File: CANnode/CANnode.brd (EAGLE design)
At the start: 59.8 x 57.7 mm, 244 parts, among them IC1 ISO1050DUB, IC2 ISO1050DUB, Q1 FDV302P, Q3 FDV302P, U1 LM324PW, U10 FT2232HL, U11 93LC56C-I/SN, U2 TPS70445_PWP_24, U3 LM324PW, U4 LM324PW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

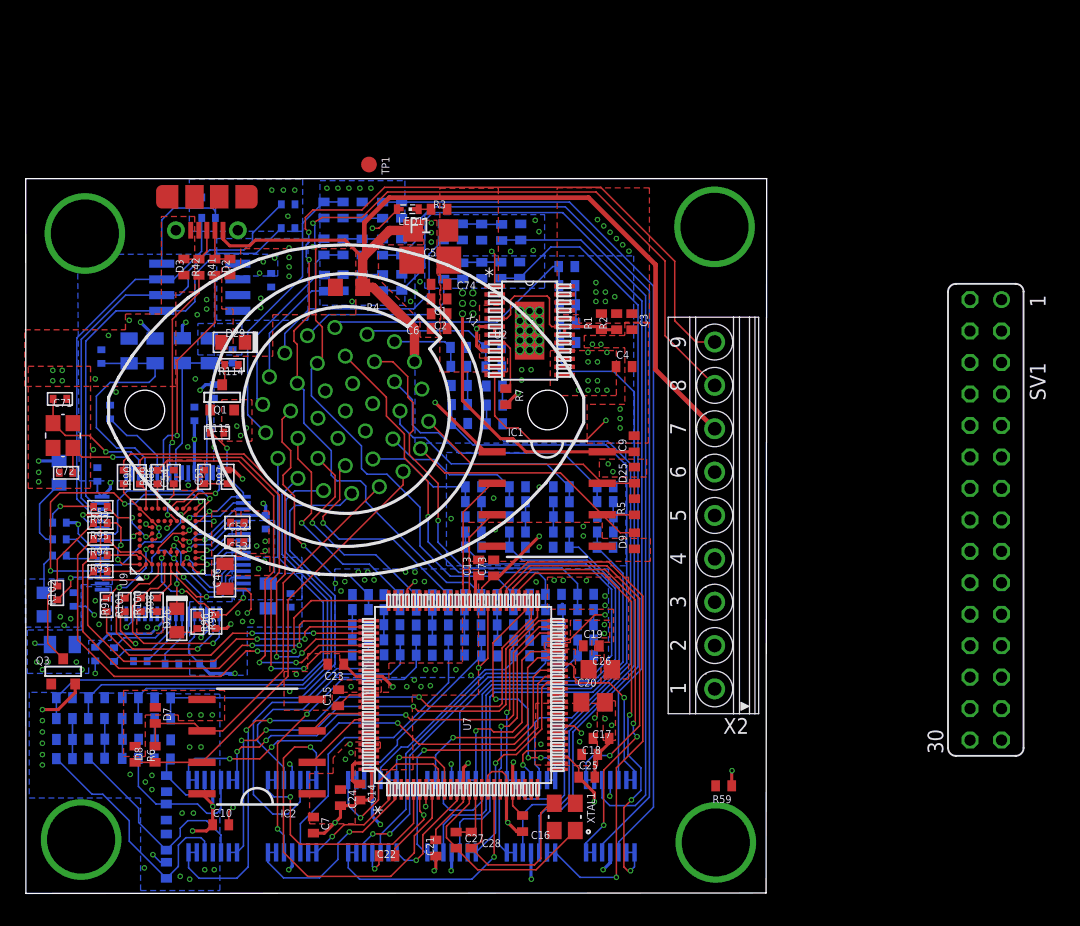
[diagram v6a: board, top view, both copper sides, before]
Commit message: Finished Debug headers
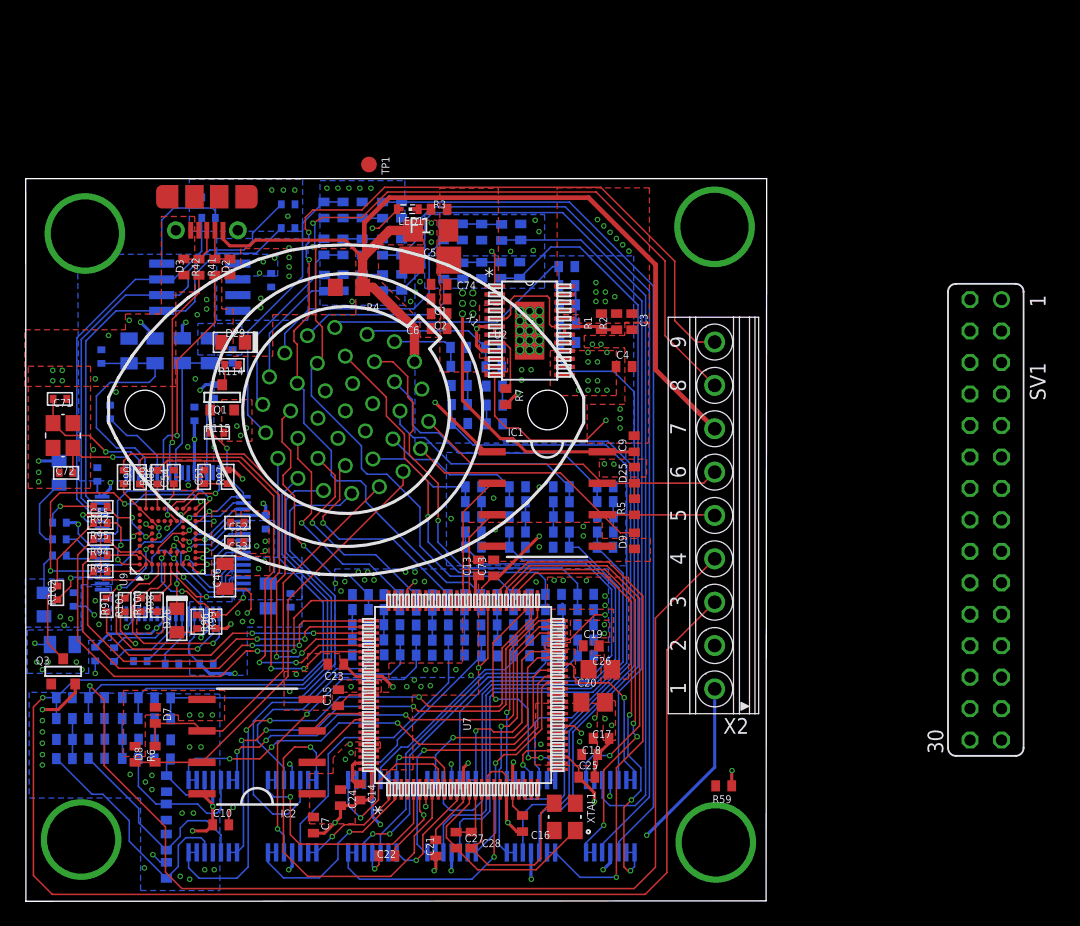
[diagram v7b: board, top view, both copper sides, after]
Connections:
- removed net N$44: X2.6
- removed net N$69: X2.5
- removed net N$70: X2.4
- removed net N$71: X2.3
- removed net N$72: X2.2
- net +5V: now also X2.1
- net A2_IN: now also X2.4
- net A3_IN: now also X2.3
- net CAN1H: now also X2.6
- net CAN1L: now also X2.5
- net GND: now also X2.2; no longer X2.1
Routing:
- net A3_IN: track 42.3 -> 134.0 mm, vias 0 -> 1
- net A2_IN: track 39.0 -> 125.2 mm, vias 0 -> 1
- net +5V: track 40.4 -> 54.4 mm, vias 13 -> 14
- net CAN1H: track 19.9 -> 26.8 mm
- net CAN1L: track 22.7 -> 29.2 mm
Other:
- board size 59.8 x 57.7 mm -> 59.8 x 58.3 mm
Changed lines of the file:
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@@
 <setting verticaltext="up"/>
 </settings>
-<grid distance="3" unitdist="mil" unit="mil" style="lines" multiple="1" display="no" altdistance="0.025" altunitdist="inch" altunit="mil"/>
+<grid distance="1" unitdist="mil" unit="mil" style="lines" multiple="1" display="no" altdistance="0.025" altunitdist="inch" altunit="mil"/>
 <layers>
 <layer number="1" name="Top" color="12" fill="1" visible="yes" active="yes"/>
@@
 <board>
 <plain>
-<wire x1="0.001153125" y1="-0.000778125" x2="59.747884375" y2="0.034490625" width="0" layer="20"/>
-<wire x1="59.747884375" y1="0.034490625" x2="59.795128125" y2="57.6990375" width="0" layer="20"/>
+<wire x1="0.001153125" y1="-0.635778125" x2="59.747884375" y2="-0.600509375" width="0" layer="20"/>
+<wire x1="59.747884375" y1="-0.600509375" x2="59.795128125" y2="57.6990375" width="0" layer="20"/>
 <wire x1="59.795128125" y1="57.6990375" x2="-0.01470625" y2="57.694140625" width="0" layer="20"/>
-<wire x1="-0.01470625" y1="57.694140625" x2="0.001153125" y2="-0.000778125" width="0" layer="20"/>
+<wire x1="-0.01470625" y1="57.694140625" x2="0.001153125" y2="-0.635778125" width="0" layer="20"/>
 </plain>
 <attributes>
@@
 <wire x1="46.52205625" y1="33.10653125" x2="49.1140625" y2="33.10653125" width="0.127" layer="1"/>
 <wire x1="49.1140625" y1="33.10653125" x2="49.120021875" y2="33.114165625" width="0.127" layer="1"/>
+<contactref element="X2" pad="6"/>
+<wire x1="49.120021875" y1="33.114165625" x2="54.705665625" y2="33.114165625" width="0.127" layer="1"/>
+<wire x1="54.705665625" y1="33.114165625" x2="55.599" y2="34.0075" width="0.127" layer="1"/>
 </signal>
 <signal name="CAN1L">
@@
 <wire x1="49.124909375" y1="30.55805" x2="46.5305375" y2="30.55805" width="0.127" layer="1"/>
 <wire x1="46.5305375" y1="30.55805" x2="46.52205625" y2="30.56653125" width="0.127" layer="1"/>
+<contactref element="X2" pad="5"/>
+<wire x1="49.124909375" y1="30.55805" x2="55.54845" y2="30.55805" width="0.127" layer="1"/>
+<wire x1="55.54845" y1="30.55805" x2="55.599" y2="30.5075" width="0.127" layer="1"/>
 </signal>
 <signal name="CAN2L">
@@
 <vertex x="31.40661875" y="36.35145"/>
 </polygon>
-<via x="47.38321875" y="34.04005" extent="1-16" drill="0.254"/>
-<via x="47.00221875" y="34.67505" extent="1-16" drill="0.254"/>
+<via x="47.45941875" y="34.64965" extent="1-16" drill="0.254"/>
+<via x="46.69741875" y="34.67505" extent="1-16" drill="0.254"/>
 <polygon width="0.127" layer="16">
 <vertex x="33.94661875" y="35.58945"/>
@@
 <wire x1="28.494615625" y1="53.694825" x2="27.97409375" y2="53.694825" width="0.127" layer="1"/>
 <wire x1="27.97409375" y1="53.694825" x2="27.969775" y2="53.69050625" width="0.127" layer="1"/>
-<contactref element="X2" pad="1"/>
 <wire x1="56.97505625" y1="8.685421875" x2="56.97505625" y2="9.88345625" width="0.254" layer="1"/>
 <wire x1="56.97505625" y1="9.88345625" x2="56.9976" y2="9.906" width="0.254" layer="1"/>
 <via x="56.9976" y="9.906" extent="1-16" drill="0.254"/>
+<contactref element="X2" pad="2"/>
 <wire x1="43.077059375" y1="47.518071875" x2="43.48156875" y2="49.00254375" width="0" layer="19" extent="1-16"/>
 <wire x1="43.48156875" y1="41.85254375" x2="40.77921875" y2="42.26965" width="0" layer="19" extent="1-1"/>
@@
 <vertex x="12.00101875" y="11.12925"/>
 <vertex x="12.00101875" y="0.30885"/>
-<vertex x="50.86301875" y="0.30885"/>
-<vertex x="50.86301875" y="5.92225"/>
+<vertex x="52.08221875" y="0.30885"/>
+<vertex x="52.08221875" y="5.92225"/>
 <vertex x="25.36141875" y="5.92225"/>
 <vertex x="25.36141875" y="42.67605"/>
@@
 <wire x1="38.31541875" y1="36.70705" x2="35.24201875" y2="39.78045" width="0.254" layer="1"/>
 <wire x1="35.24201875" y1="39.78045" x2="35.24201875" y2="46.79085" width="0.254" layer="1"/>
+<contactref element="X2" pad="1"/>
+<wire x1="55.599" y1="16.5075" x2="55.599" y2="10.1838" width="0.254" layer="16"/>
+<wire x1="55.599" y1="10.1838" x2="50.1142" y2="4.699" width="0.254" layer="16"/>
+<via x="50.1142" y="4.699" extent="1-16" drill="0.254"/>
 </signal>
 <signal name="N$45">
@@
 <wire x1="5.0440875" y1="15.80144375" x2="5.0440875" y2="14.115978125" width="0.127" layer="16"/>
 <wire x1="5.057078125" y1="15.80144375" x2="6.099884375" y2="16.84425" width="0.127" layer="16"/>
+<contactref element="X2" pad="4"/>
+<wire x1="55.599" y1="27.0075" x2="50.8176625" y2="22.2261625" width="0.127" layer="1"/>
+<wire x1="50.8176625" y1="22.2261625" x2="50.8176625" y2="2.11125625" width="0.127" layer="1"/>
+<wire x1="50.8176625" y1="2.11125625" x2="49.09720625" y2="0.3908" width="0.127" layer="1"/>
+<wire x1="49.09720625" y1="0.3908" x2="12.597834375" y2="0.3908" width="0.127" layer="1"/>
+<wire x1="12.597834375" y1="0.3908" x2="11.268334375" y2="1.7203" width="0.127" layer="1"/>
+<wire x1="11.268334375" y1="1.7203" x2="11.268334375" y2="5.37065" width="0.127" layer="1"/>
+<wire x1="11.268334375" y1="5.37065" x2="6.3139125" y2="10.325071875" width="0.127" layer="1"/>
+<wire x1="6.3139125" y1="10.325071875" x2="6.3139125" y2="15.0622" width="0.127" layer="1"/>
+<via x="5.16174375" y="16.7591125" extent="1-16" drill="0.254"/>
+<wire x1="6.3139125" y1="15.0622" x2="6.3139125" y2="15.58154375" width="0.127" layer="1"/>
+<wire x1="5.16174375" y1="16.7591125" x2="5.16174375" y2="15.906109375" width="0.127" layer="16"/>
+<wire x1="5.16174375" y1="15.906109375" x2="5.057078125" y2="15.80144375" width="0.127" layer="16"/>
+<wire x1="5.16174375" y1="16.7591125" x2="6.3139125" y2="15.60694375" width="0.127" layer="1"/>
+<wire x1="6.3139125" y1="15.60694375" x2="6.3139125" y2="15.58154375" width="0.127" layer="1"/>
 </signal>
 <signal name="A3_IN">
@@
 <wire x1="2.45846875" y1="15.798040625" x2="3.885678125" y2="17.22525" width="0.127" layer="16"/>
 <wire x1="24.00165625" y1="18.868746875" x2="22.358159375" y2="17.22525" width="0.127" layer="16"/>
+<contactref element="X2" pad="3"/>
+<wire x1="51.7398" y1="19.6483" x2="51.7398" y2="1.6764" width="0.127" layer="1"/>
+<wire x1="51.7398" y1="1.6764" x2="49.9872" y2="-0.0762" width="0.127" layer="1"/>
+<wire x1="49.9872" y1="-0.0762" x2="2.1336" y2="-0.0762" width="0.127" layer="1"/>
+<wire x1="2.1336" y1="-0.0762" x2="0.6096" y2="1.4478" width="0.127" layer="1"/>
+<wire x1="0.6096" y1="1.4478" x2="0.6096" y2="15.05169375" width="0.127" layer="1"/>
+<wire x1="0.6096" y1="15.05169375" x2="1.361340625" y2="15.803434375" width="0.127" layer="1"/>
+<via x="1.361340625" y="15.803434375" extent="1-16" drill="0.254"/>
+<wire x1="1.361340625" y1="15.803434375" x2="2.453075" y2="15.803434375" width="0.127" layer="16"/>
+<wire x1="2.453075" y1="15.803434375" x2="2.45846875" y2="15.798040625" width="0.127" layer="16"/>
+<wire x1="55.599" y1="23.5075" x2="51.7398" y2="19.6483" width="0.127" layer="1"/>
 </signal>
 <signal name="A7_IN">
@@
 <signal name="N$9">
 </signal>
-<signal name="N$44">
-<contactref element="X2" pad="6"/>
-</signal>
-<signal name="N$69">
-<contactref element="X2" pad="5"/>
-</signal>
-<signal name="N$70">
-<contactref element="X2" pad="4"/>
-</signal>
-<signal name="N$71">
-<contactref element="X2" pad="3"/>
-</signal>
-<signal name="N$72">
-<contactref element="X2" pad="2"/>
-</signal>
 </signals>

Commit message: Updated silkscreen, some ground pours, added pullup on jtag select line.
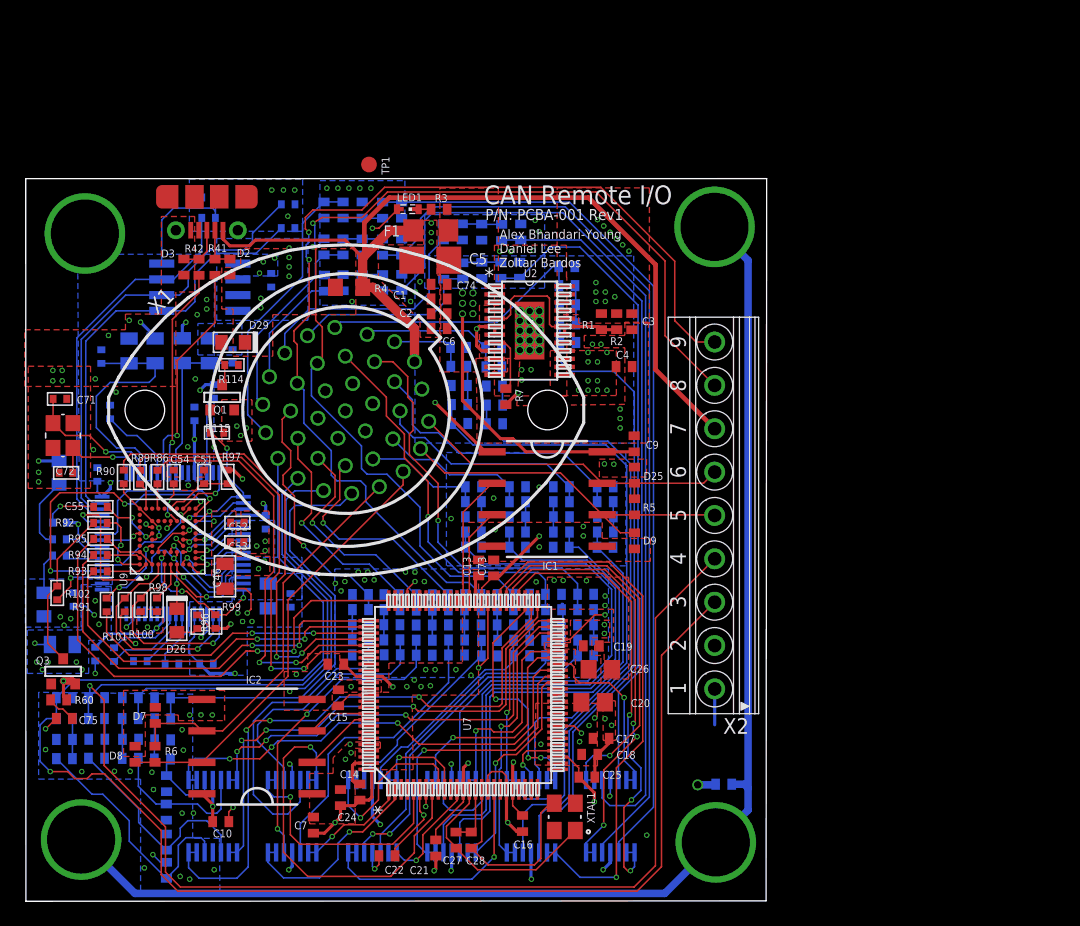
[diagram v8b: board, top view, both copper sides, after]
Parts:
- removed SV1: (no value), con-lsta:FE15-2
- added C75: 100nF, rcl:C0402
- added R60: 39K, resistor:R0402
- moved C10 0.25 mm to (15.7, 5.79)
- moved R59 0.13 mm to (56.3, 8.81), flipped to the bottom
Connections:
- net +3V3: now also R60.2
- net GND: now also C75.2, U2.EPAD
- net JTAG_SEL: now also C75.1, R60.1; no longer Q3.3
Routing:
- net CGND: track 0.00 -> 108.1 mm
- net GND: track 101.2 -> 85.7 mm, vias 137 -> 133
- net +5V: track 54.4 -> 41.1 mm, vias 14 -> 13
- net A3_IN: track 134.0 -> 127.6 mm
- net JTAG_SEL: track 0.00 -> 2.51 mm
- net +3V3: track 82.8 -> 81.6 mm
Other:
- board text added: "Alex Bhandari-Young Daniel Lee Zoltan Bardos"
- board text added: "CAN Remote I/O"
- board text added: "CGND<->GND"
- board text added: "P/N: PCBA-001 Rev1"
